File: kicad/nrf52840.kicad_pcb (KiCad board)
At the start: 2 copper layers, 40.5 x 51.5 mm, 16 parts, among them J1 Conn_01x02, J2 Conn_01x04, J3 Conn_01x06, J4 Conn_01x10, SW1 SW_Push, U1 NRF52840_MS88SF2, U2 AMS1117-3.3, U3 LM2902

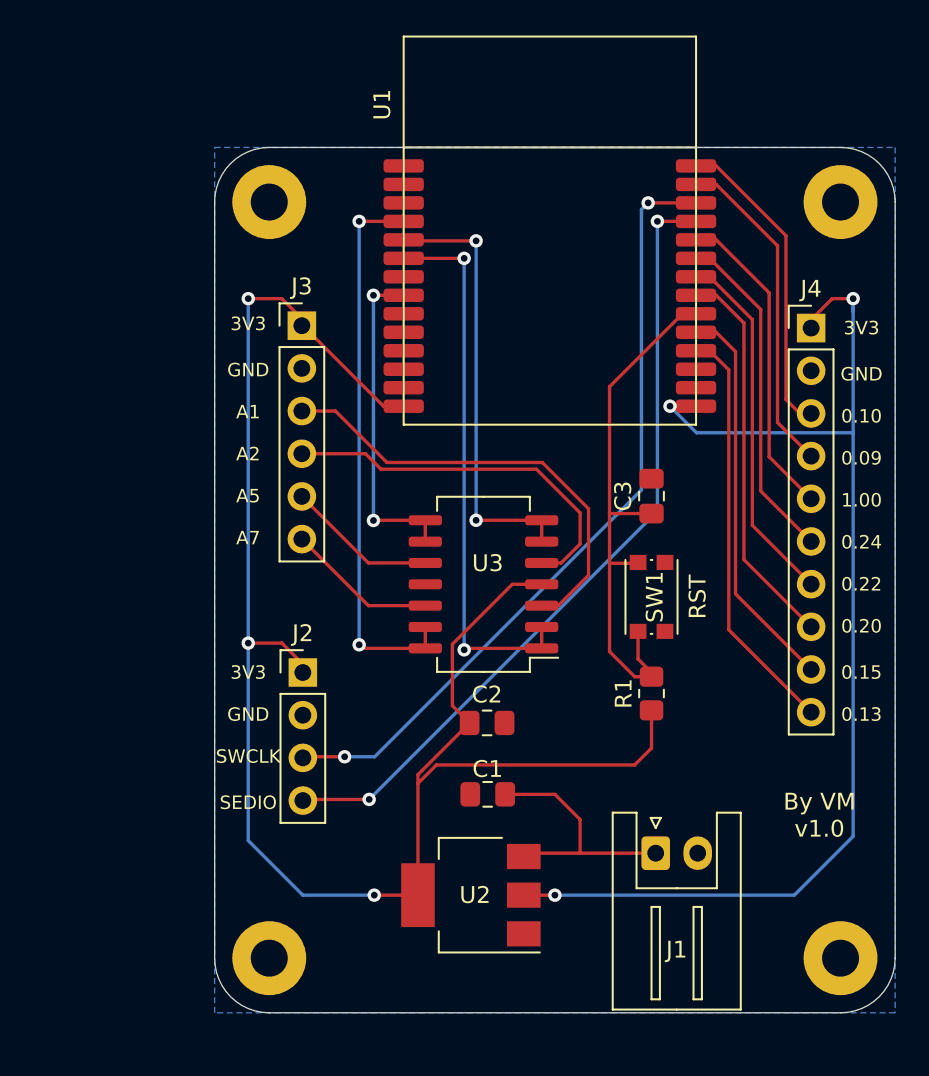
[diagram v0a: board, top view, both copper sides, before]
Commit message: add resistors for input analogs
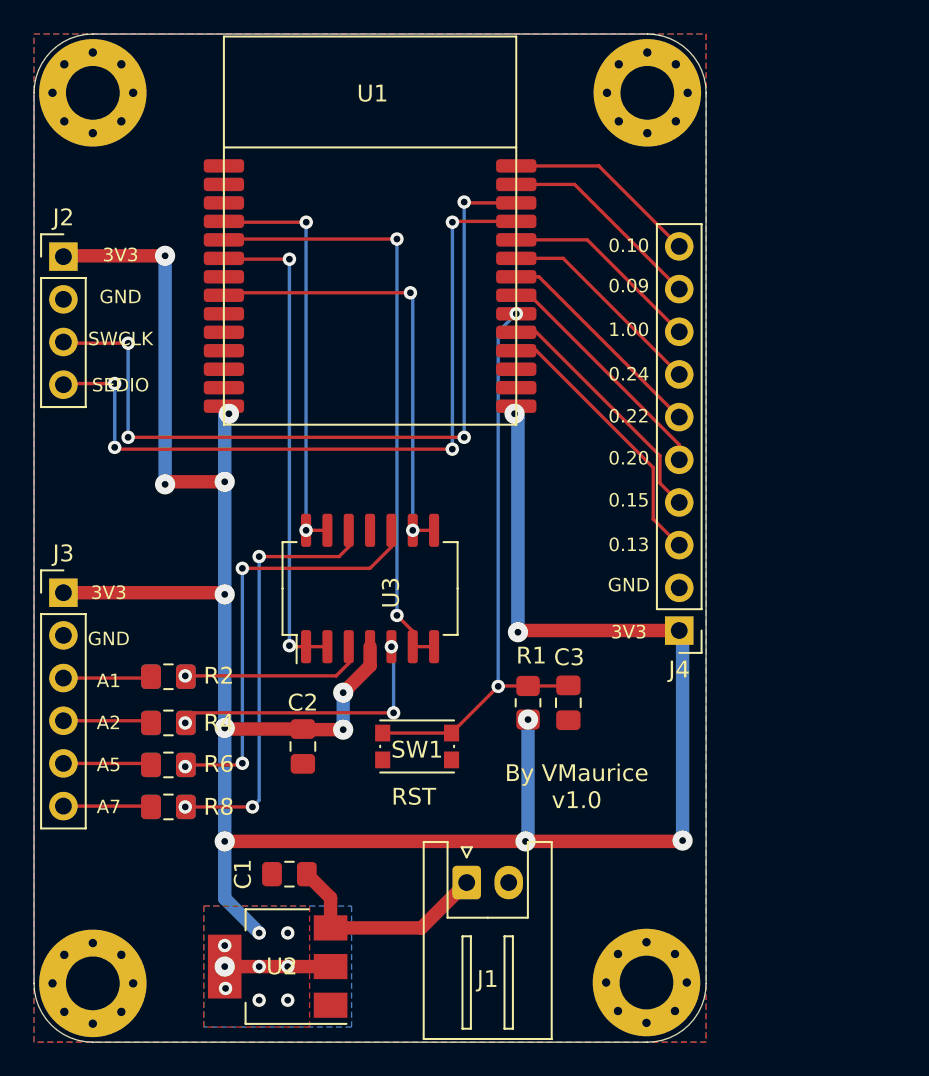
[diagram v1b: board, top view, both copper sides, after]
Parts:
- added R2: R, Capacitor_SMD:C_0805_2012Metric_Pad1.18x1.45mm_HandSolder, F.Cu at (33.0, 67.2)
- added R3: R, Capacitor_SMD:C_0805_2012Metric_Pad1.18x1.45mm_HandSolder, B.Cu at (33.0, 67.2)
- added R4: R, Capacitor_SMD:C_0805_2012Metric_Pad1.18x1.45mm_HandSolder, F.Cu at (33.0, 70.0)
- added R5: R, Capacitor_SMD:C_0805_2012Metric_Pad1.18x1.45mm_HandSolder, B.Cu at (33.0, 70.0)
- added R6: R, Capacitor_SMD:C_0805_2012Metric_Pad1.18x1.45mm_HandSolder, F.Cu at (33.0, 72.5)
- added R7: R, Capacitor_SMD:C_0805_2012Metric_Pad1.18x1.45mm_HandSolder, B.Cu at (33.0, 72.5)
- added R8: R, Capacitor_SMD:C_0805_2012Metric_Pad1.18x1.45mm_HandSolder, F.Cu at (33.0, 75.0)
- added R9: R, Capacitor_SMD:C_0805_2012Metric_Pad1.18x1.45mm_HandSolder, B.Cu at (33.0, 75.0)
- C3: value 100 nF -> 1 uF
- H1, H2, H3, H4: value 2.2mm for M2 -> 3.2mm for M3; footprint MountingHole:MountingHole_2.2mm_M2_Pad -> MountingHole:MountingHole_3.2mm_M3_Pad_Via
- moved J2 28.6 mm to (26.8, 42.2)
- moved J3 21.3 mm to (26.8, 62.2)
- moved J4 19.6 mm to (63.4, 64.5), turned to 180 degrees
- moved SW1 16.5 mm to (47.8, 71.4), turned to 0 degrees
- moved C3 13.3 mm to (56.8, 68.8), turned to 270 degrees
- moved H2 13.2 mm to (61.5, 32.5)
- moved C1 12.7 mm to (40.2, 79.0)
- moved H1 12.3 mm to (28.5, 32.5)
- moved U2 12.3 mm to (39.5, 84.5)
- moved H4 11.6 mm to (61.5, 85.5)
- moved J1 11.4 mm to (50.8, 79.5)
- moved C2 11.1 mm to (41.0, 71.4), turned to 270 degrees
- moved U1 10.7 mm to (36.3, 52.2)
- moved H3 10.6 mm to (28.5, 85.5)
- moved R1 7.37 mm to (54.4, 68.8)
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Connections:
- J4 pad 10: /P0.13 -> /P0.10
- J4 pad 3: /P0.10 -> /P0.13
- J4 pad 4: /P0.09 -> /P0.15
- J4 pad 5: /P1.00 -> /P0.20
- J4 pad 6: /P0.24 -> /P0.22
- J4 pad 7: /P0.22 -> /P0.24
- J4 pad 8: /P0.20 -> /P1.00
- J4 pad 9: /P0.15 -> /P0.09
- U3 pad 10: /ANA_2 -> Net-(R6-Pad1)
- U3 pad 12: /ANA_3 -> Net-(R8-Pad1)
- U3 pad 3: /ANA_0 -> Net-(R2-Pad1)
- U3 pad 5: /ANA_1 -> Net-(R4-Pad1)
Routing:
- net Net-(R8-Pad1): track 0.00 -> 25.6 mm, vias 0 -> 3
- net Net-(R6-Pad1): track 0.00 -> 25.4 mm, vias 0 -> 3
- net /ANA_0: track 27.0 -> 5.25 mm
- net /ANA_1: track 22.6 -> 5.27 mm
- net Net-(R4-Pad1): track 0.00 -> 16.6 mm, vias 0 -> 3
- net +3V3: track 170.5 -> 154.0 mm, vias 6 -> 23
- net Net-(R2-Pad1): track 0.00 -> 11.0 mm, vias 0 -> 1
- net /ADC_2: track 26.1 -> 36.2 mm
- net /P0.20: track 23.3 -> 14.3 mm
- net /P0.15: track 23.6 -> 14.9 mm
- net /ADC_0: track 33.1 -> 24.5 mm
- net /P0.13: track 24.8 -> 16.3 mm
- net /P0.22: track 21.6 -> 13.2 mm
- net /P0.24: track 20.2 -> 12.6 mm
- net /P0.09: track 19.7 -> 12.3 mm
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- added copper zone on B.Cu, net +3V3
- added copper zone on F.Cu, net +3V3
- added copper zone on F.Cu, net GND
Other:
- board size 40.5 x 51.5 mm -> 40 x 60 mm
- net class power added: clearance 0.2, trace_width 0.8, via_dia 1.2, via_drill 0.4
- board text added: "By VMaurice v1.0"
- board text removed: "By VM v1.0"
